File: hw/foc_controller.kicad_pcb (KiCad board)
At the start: 4 copper layers, 45 x 45 mm, 118 parts, among them J1 XT30PW-F bus IN, J2 XT30PW-F bus OUT, J3 MOTOR_A, J4 MOTOR_B, J5 MOTOR_C, J6 SWD, J7 CAN IN, J8 CAN OUT, J9 USB-C, Q1 BSC026N08NS5, Q2 BSC026N08NS5, Q3 BSC026N08NS5, Q4 BSC026N08NS5, Q5 BSC026N08NS5, Q6 BSC026N08NS5, SW1 TERM, U1 LM5008A, U2 AP2112K-3.3, U3 DRV8353S, U4 STM32G474CEU6, U5 AS5047P, U6 TCAN3413, U7 USBLC6-2SC6, Y1 16MHz 9pF

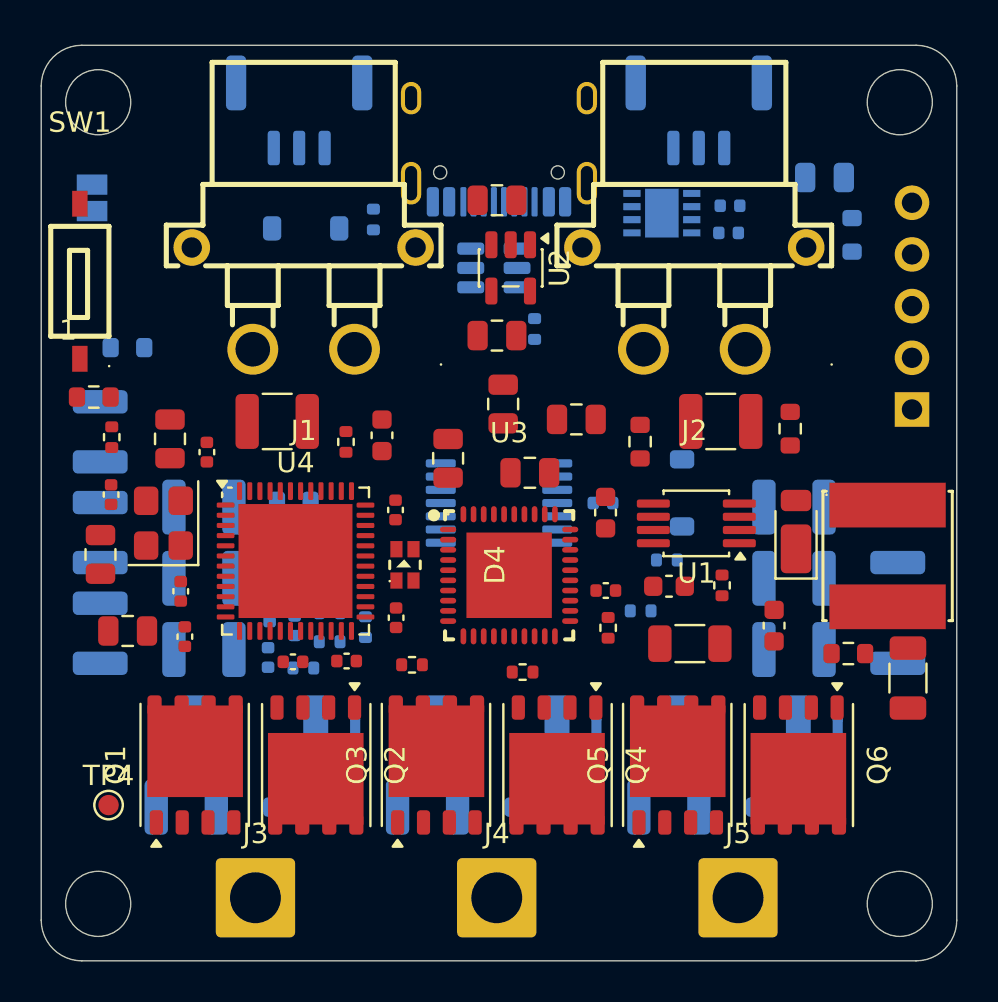
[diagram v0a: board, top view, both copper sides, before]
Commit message: Route the 6-layer board and finalize parts for ordering
The 45 x 45 mm board is fully routed on six layers (F / GND / SIG /
SIG / PWR / B, 2 oz outer, 1 oz inner): DRC 0 errors, 0 unconnected,
schematic parity 0. Four layers could not route the DRV-to-MCU links
without moving the power or input stage.

- Encoder shares the DRV8353's SPI3 bus, as on the PoC; PA5-PA7 are
  unused. R25 pulls DRV nSCS up, since the DRV's logic inputs have an
  internal pull-down. The SDO / MISO pin-type warning is an ERC
  exclusion with a note.
- MCU is now the STM32G473CEU6: the G474 without the unused HRTIM,
  checked pin for pin against both datasheets, in stock and cheaper.
- Male XT30PW-M power connectors, HCS1206 shunts, SWD pads at the
  board edge.
- Design doc and review notes updated for the new stack-up, shared
  bus and MCU.

Co-Authored-By: Claude Opus 5.5 <noreply@anthropic.com>
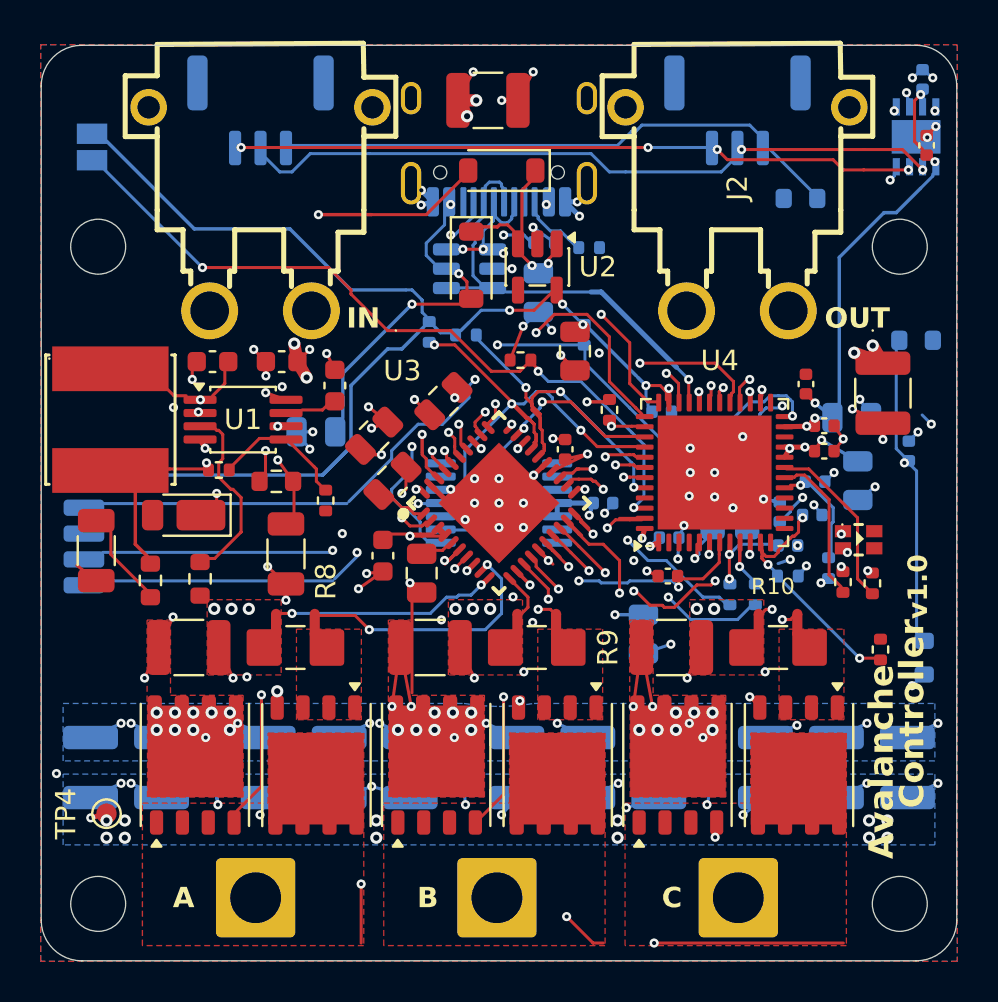
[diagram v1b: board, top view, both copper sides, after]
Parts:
- removed R21: 120 1%, Resistor_SMD:R_0603_1608Metric
- removed SW1: TERM, foc_controller:SW-SMD_1.27-1P-TPPT
- added R25: 10k 1%, Resistor_SMD:R_0402_1005Metric, F.Cu at (130.4, 120.4)
- C1, C42, C5, C9, D2, D3, NT1, NT2, NT3, NT4, NT5, NT6: moved to F.Cu
- C16, C25, C26, C27, C29, C31, C32, C33, Y1: moved to B.Cu
- DBUG: renamed from J6; footprint Connector_PinHeader_2.54mm:PinHeader_1x05_P2.54mm_Vertical -> foc_controller:SWD_Pads_1x05_P1.27mm_SMD
- H1, H2, H3, H4: value M3 -> M2.5; footprint MountingHole:MountingHole_3.2mm_M3 -> MountingHole:MountingHole_2.7mm_M2.5
- J1: value XT30PW-F bus IN -> XT30PW-M bus IN; footprint foc_controller:CONN-TH_XT30PW-F-1 -> foc_controller:CONN-TH_XT30PW-M-1
- J2: value XT30PW-F bus OUT -> XT30PW-M bus OUT; footprint foc_controller:CONN-TH_XT30PW-F-1 -> foc_controller:CONN-TH_XT30PW-M-1
- R10, R8, R9: value 1m 1% 3W -> 1m 1% 2W; footprint Resistor_SMD:R_2512_6332Metric -> foc_controller:R_1206_Shunt_HCS1206; moved to F.Cu
- U4: value STM32G474CEU6 -> STM32G473CEU6
- moved R17 42.0 mm to (145.9, 132.6), turned to 90 degrees
- moved DBUG 41.2 mm to (104.6, 126.5), turned to -90 degrees
- moved C15 40.4 mm to (105.2, 127.3), turned to -90 degrees
- moved L1 38.8 mm to (105.9, 120.9)
- moved C31 37.5 mm to (142.3, 120.8), turned to 0 degrees
- moved C29 36.6 mm to (142.6, 123.9), turned to -90 degrees
- moved R5 34.5 mm to (107.9, 128.8), turned to -90 degrees
- moved R18 31.6 mm to (145.5, 117.0)
- moved C33 31.1 mm to (136.9, 122.2), turned to 0 degrees
- moved C38 30.9 mm to (145.1, 122.4), turned to 90 degrees
- moved C14 30.5 mm to (110.9, 118.0), turned to 0 degrees
- moved D1 30.1 mm to (109.5, 125.6), turned to 180 degrees
- moved R2 29.9 mm to (110.3, 128.7), turned to -90 degrees
- moved C30 28.1 mm to (141.0, 122.5), turned to 0 degrees
- moved C43 28.0 mm to (116.0, 121.5), turned to 180 degrees
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- renumbered J3 to A, J4 to B, J5 to C, J7 to CAN1, J8 to CAN2
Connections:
- U4 pad 13: /DRV_SCLK -> unconnected-(U4-PA5-Pad13)
- U4 pad 14: /DRV_SDO -> unconnected-(U4-PA6-Pad14)
- U4 pad 15: /DRV_SDI -> unconnected-(U4-PA7-Pad15)
- U4 pad 22: /DRV_nFAULT -> unconnected-(U4-PB10-Pad22)
- U4 pad 24: /DRV_EN -> /ENC_CS
- U4 pad 25: /ENC_CS -> unconnected-(U4-PB12-Pad25)
- U4 pad 26: /INLA -> /INLC
- U4 pad 28: /INLC -> /INLA
- U4 pad 29: unconnected-(U4-PC6-Pad29) -> /DRV_EN
- U4 pad 30: /INHA -> /INHC
- U4 pad 32: /INHC -> /INHA
- U4 pad 38: /CAN_TX -> /DRV_nSCS
- U4 pad 39: /ENC_SCK -> /DRV_SCLK
- U4 pad 40: /ENC_MISO -> /DRV_SDO
- U4 pad 42: unconnected-(U4-PB4-Pad42) -> /CAN_TX
- U4 pad 43: /ENC_MOSI -> /DRV_SDI
- U4 pad 44: unconnected-(U4-PB6-Pad44) -> /DRV_nFAULT
- U4 pad 45: /DRV_nSCS -> unconnected-(U4-PB7-Pad45)
- U5 pad 2: /ENC_SCK -> /DRV_SCLK
- U5 pad 3: /ENC_MISO -> /DRV_SDO
- U5 pad 4: /ENC_MOSI -> /DRV_SDI
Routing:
- net +3V3: track 0.00 -> 99.1 mm, vias 0 -> 20
- net GND: track 0.00 -> 80.4 mm, vias 0 -> 111
- net VBUS: track 0.00 -> 61.4 mm, vias 0 -> 56
- net /CAN_STB: track 0.00 -> 36.9 mm, vias 0 -> 4
- net /MCU/SWDIO: track 0.00 -> 36.5 mm, vias 0 -> 2
- net /MCU/BOOT0: track 0.00 -> 36.1 mm, vias 0 -> 3
- net /MCU/SWCLK: track 0.00 -> 34.1 mm, vias 0 -> 2
- net /MCU/NRST: track 0.00 -> 33.6 mm, vias 0 -> 3
- net /Comms/CAN_L: track 0.00 -> 33.5 mm, vias 0 -> 2
- net /Comms/CAN_H: track 0.00 -> 32.7 mm, vias 0 -> 4
- net /CAN_RX: track 0.00 -> 31.7 mm, vias 0 -> 2
- net /ENC_CS: track 0.00 -> 31.6 mm, vias 0 -> 3
- net /PHASE_C: track 0.00 -> 31.0 mm, vias 0 -> 2
- net /CAN_TX: track 0.00 -> 29.0 mm, vias 0 -> 2
- net /Power/+5V_BUCK: track 0.00 -> 27.5 mm, vias 0 -> 2
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- added copper zone on In4.Cu, net +3V3
- added copper zone on F.Cu, net /Bridge/SHUNT_A
- added copper zone on F.Cu, net /Bridge/SHUNT_B
- added copper zone on F.Cu, net /Bridge/SHUNT_C
- added copper zone on F.Cu, net /PHASE_A
- added copper zone on F.Cu, net /PHASE_B
- added copper zone on F.Cu, net /PHASE_C
- added copper zone on B.Cu, net GND
- added copper zone on F.Cu, net GND
- added copper zone on In1.Cu, net GND
- added copper zone on B.Cu, net VBUS
- added copper zone on F.Cu, net VBUS
- added copper zone on In4.Cu, net VBUS
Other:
- copper layers 4 -> 6
- board text added: "A"
- board text added: "Avalanche"
- board text added: "B"
- board text added: "C"
- board text added: "Controller_{v1.0}"
- board text added: "IN"
- board text added: "OUT"

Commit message: Rename the GND test pad and keep silkscreen labels as text
TP4 is the only test pad left, so it becomes TP1 in the schematic,
board and docs.

The motor, SWD and CAN labels (A, B, C, DBUG, CAN1, CAN2) had been set
by renaming the reference designators on the board. That broke
schematic parity, and it would have dropped J7 and J8 from JLC
assembly, because the BOM lists them by their schematic references.
J3-J8 keep their references, hidden on silk, and each label is now a
text item on its footprint with the same position, size and layer.
The plotted silkscreen is identical to before.

Co-Authored-By: Claude Opus 5.5 <noreply@anthropic.com>
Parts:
- renumbered A to J3, B to J4, C to J5, DBUG to J6, CAN1 to J7, CAN2 to J8, TP4 to TP1
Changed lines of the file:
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@@
 		(descr "Soldered wire connection, for a single 2 mm² wire, reinforced insulation, conductor diameter 2mm, outer diameter 3.9mm, size source Multi-Contact FLEXI-xV 2.0 (https://www.staubli.com/content/dam/ecs/catalogs-brochures/TM/CAB-Main-11014119-en.pdf#page=11), bend radius 3 times outer diameter")
 		(tags "connector wire 2sqmm")
-		(property "Reference" "C"
+		(property "Reference" "J5"
 			(at -3.26 0 0)
 			(layer "F.SilkS")
+			(hide yes)
 			(effects
 				(font
@@
 			(layer "F.Fab")
 		)
+		(fp_text user "C"
+			(at -3.26 0 0)
+			(layer "F.SilkS")
+			(effects
+				(font
+					(size 1 1)
+					(thickness 0.2)
+				)
+			)
+		)
 		(fp_text user "${REFERENCE}"
 			(at 0 0 0)
@@
 		(descr "Soldered wire connection, for a single 2 mm² wire, reinforced insulation, conductor diameter 2mm, outer diameter 3.9mm, size source Multi-Contact FLEXI-xV 2.0 (https://www.staubli.com/content/dam/ecs/catalogs-brochures/TM/CAB-Main-11014119-en.pdf#page=11), bend radius 3 times outer diameter")
 		(tags "connector wire 2sqmm")
-		(property "Reference" "B"
+		(property "Reference" "J4"
 			(at -3.4 0 0)
 			(layer "F.SilkS")
+			(hide yes)
 			(effects
 				(font
@@
 			(layer "F.Fab")
 		)
+		(fp_text user "B"
+			(at -3.4 0 0)
+			(layer "F.SilkS")
+			(effects
+				(font
+					(size 1 1)
+					(thickness 0.2)
+				)
+			)
+		)
 		(fp_text user "${REFERENCE}"
 			(at 0 0 0)
@@
 		(descr "SMD pad as test Point, diameter 1.0mm")
 		(tags "test point SMD pad")
-		(property "Reference" "TP4"
+		(property "Reference" "TP1"
 			(at -1.995803 -0.000001 90)
 			(layer "F.SilkS")
@@
 		(descr "Soldered wire connection, for a single 2 mm² wire, reinforced insulation, conductor diameter 2mm, outer diameter 3.9mm, size source Multi-Contact FLEXI-xV 2.0 (https://www.staubli.com/content/dam/ecs/catalogs-brochures/TM/CAB-Main-11014119-en.pdf#page=11), bend radius 3 times outer diameter")
 		(tags "connector wire 2sqmm")
-		(property "Reference" "A"
+		(property "Reference" "J3"
 			(at -3.54 0 0)
 			(layer "F.SilkS")
+			(hide yes)
 			(effects
 				(font
@@
 			(layer "F.Fab")
 		)
+		(fp_text user "A"
+			(at -3.54 0 0)
+			(layer "F.SilkS")
+			(effects
+				(font
+					(size 1 1)
+					(thickness 0.2)
+				)
+			)
+		)
 		(fp_text user "${REFERENCE}"
 			(at 0 0 0)
@@
 		(descr "Five bare SMD pads, 1.27 mm pitch, for an SWD probe: hand-solder wires or a 1.27 mm SMD header. No paste: not fitted at assembly.")
 		(tags "swd debug pads")
-		(property "Reference" "DBUG"
+		(property "Reference" "J6"
 			(at -4.44325 -0.9 0)
 			(layer "B.SilkS")
+			(hide yes)
 			(effects
 				(font
@@
 			(layer "B.CrtYd")
 		)
+		(fp_text user "DBUG"
+			(at -4.44325 -0.9 0)
+			(layer "B.SilkS")
+			(effects
+				(font
+					(size 1 1)
+					(thickness 0.15)
+				)
+				(justify mirror)
+			)
+		)
 		(fp_text user "${REFERENCE}"
 			(at 0 0 270)
@@
 		(descr "JST GH series connector, SM03B-GHS-TB (http://www.jst-mfg.com/product/pdf/eng/eGH.pdf)")
 		(tags "connector JST GH horizontal")
-		(property "Reference" "CAN2"
+		(property "Reference" "J8"
 			(at -4.22 2.8 0)
 			(layer "B.SilkS")
+			(hide yes)
 			(effects
 				(font
@@
 			(layer "B.Fab")
 		)
+		(fp_text user "CAN2"
+			(at -4.22 2.8 0)
+			(layer "B.SilkS")
+			(effects
+				(font
+					(size 1 1)
+					(thickness 0.15)
+				)
+				(justify mirror)
+			)
+		)
 		(fp_text user "${REFERENCE}"
 			(at 0 0 180)
@@
 		(descr "JST GH series connector, SM03B-GHS-TB (http://www.jst-mfg.com/product/pdf/eng/eGH.pdf)")
 		(tags "connector JST GH horizontal")
-		(property "Reference" "CAN1"
+		(property "Reference" "J7"
 			(at 3.72 2.8 0)
 			(layer "B.SilkS")
+			(hide yes)
 			(effects
 				(font
@@
 			(layer "B.Fab")
 		)
+		(fp_text user "CAN1"
+			(at 3.72 2.8 0)
+			(layer "B.SilkS")
+			(effects
+				(font
+					(size 1 1)
+					(thickness 0.15)
+				)
+				(justify mirror)
+			)
+		)
 		(fp_text user "${REFERENCE}"
